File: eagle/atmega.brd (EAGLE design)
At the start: 65.3 x 40.9 mm, 48 parts, among them IC1 TO 5V, IC2 LM339D, Q2 16MHz, U1 ATMEGA328P-AU

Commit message: Dopisanie kilku komentarzy do schematu
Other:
- board size 65.3 x 40.9 mm -> 65.3 x 43.7 mm

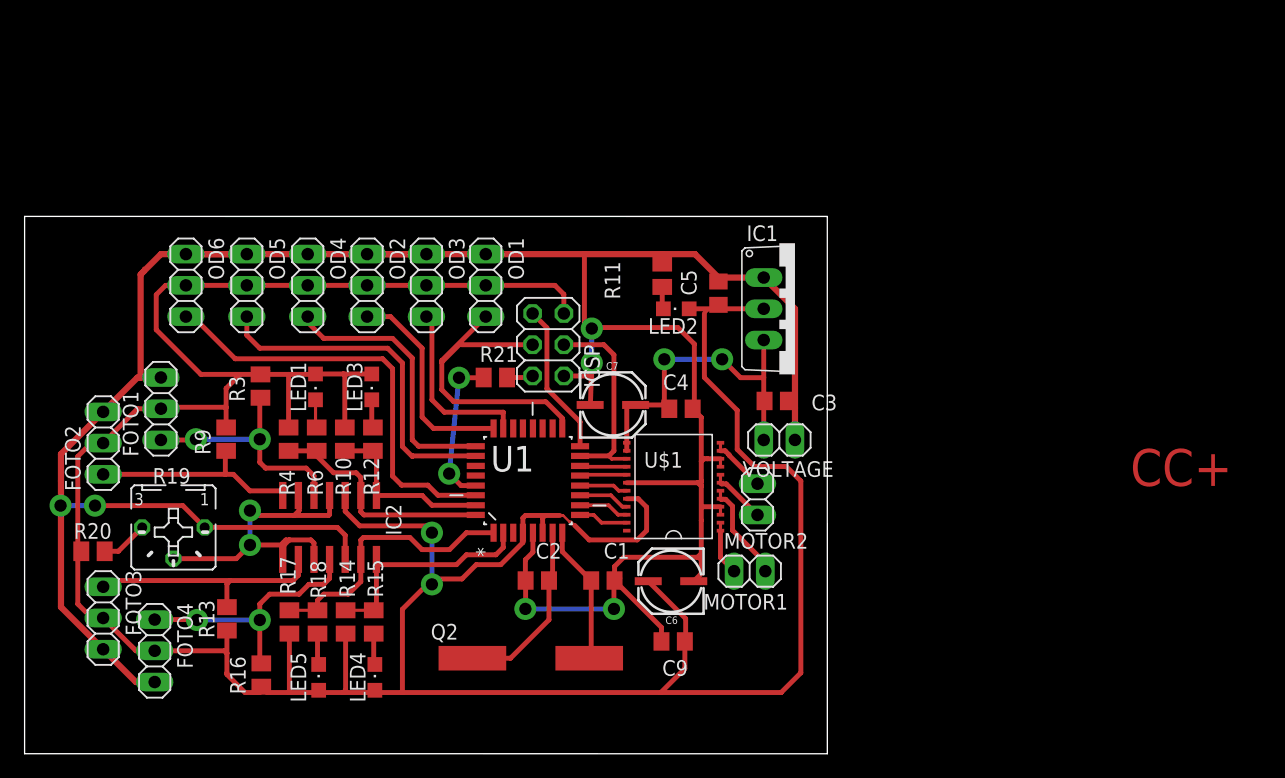
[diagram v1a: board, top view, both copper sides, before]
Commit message: usunięcie LEDów
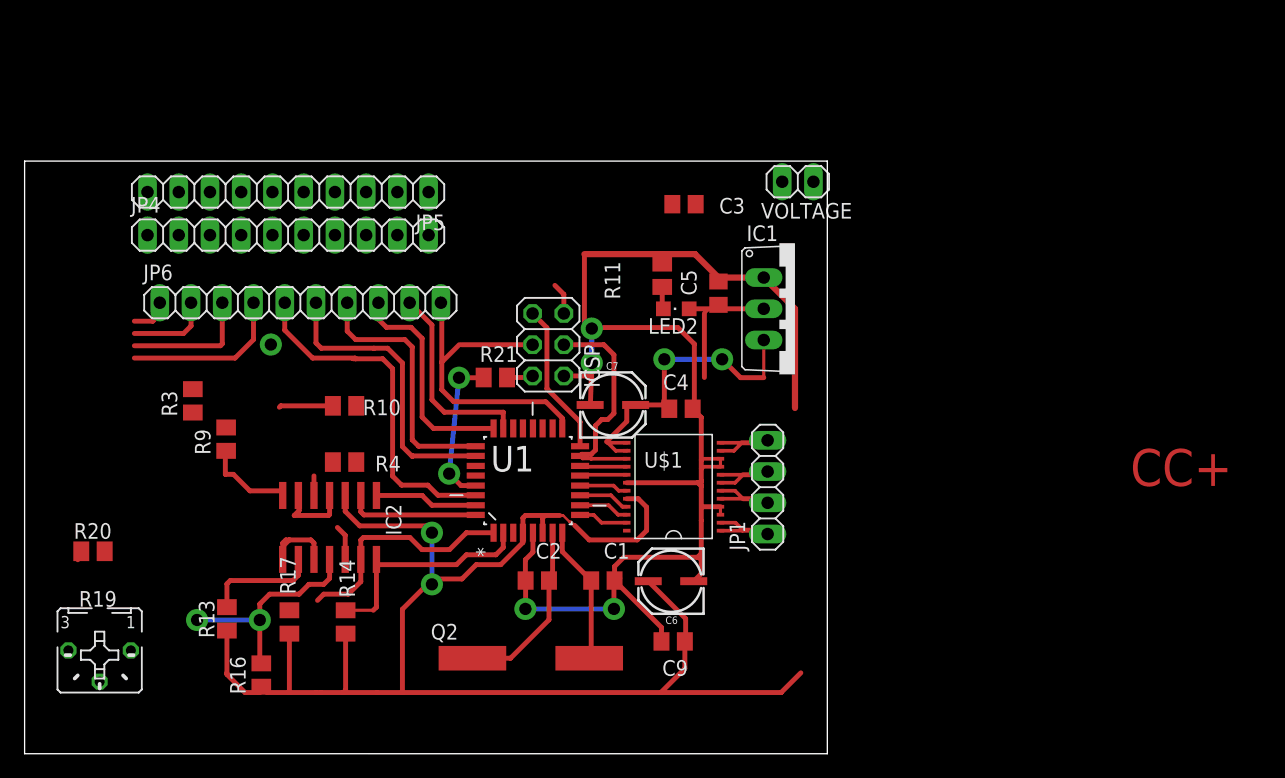
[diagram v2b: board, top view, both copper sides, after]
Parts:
- removed FOTO1, FOTO2, FOTO3, FOTO4, OD1, OD2, OD3, OD4, OD5, OD6: (no value), pinhead:1X03
- removed LED1, LED3, LED4, LED5: (no value), led:CHIPLED_0805
- removed MOTOR1, MOTOR2: (no value), pinhead:1X02
- removed R12, R15, R18, R6: 220R, resistor:M0805
- added JP1: (no value), pinhead:1X04
- added JP4, JP5, JP6: (no value), pinhead:1X10
- moved VOLTAGE 21.1 mm to (61.0, 42.3)
- moved C3 17.7 mm to (51.7, 40.5)
- moved R19 11.7 mm to (4.18, 4.23)
- moved R3 5.63 mm to (11.8, 24.5)
- moved R4 4.92 mm to (24.1, 19.5), turned to 180 degrees
- moved R10 2.71 mm to (24.1, 24.1), turned to 180 degrees
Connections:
- removed net N$2: LED3.C, R12.2
- removed net N$20: LED1.C, R6.2
- removed net N$21: LED4.C, R15.2
- removed net N$29: LED5.C, R18.2
- removed net OUTMA1: MOTOR1.2, U$1.1, U$1.2
- removed net OUTMA2: MOTOR1.1, U$1.5, U$1.6
- removed net OUTMB1: MOTOR2.1, U$1.11, U$1.12
- removed net OUTMB2: MOTOR2.2, U$1.7, U$1.8
- new net AO1: JP1.1, U$1.1, U$1.2
- new net AO2: JP1.2, U$1.5, U$1.6
- new net BO1: JP1.4, U$1.11, U$1.12
- new net BO2: JP1.3, U$1.7, U$1.8
- net CO1: now also JP6.10; no longer OD1.3
- net CO2: now also JP6.8; no longer OD2.3
- net CO3: now also JP6.9; no longer OD3.3
- net CO4: now also JP6.7; no longer OD4.3
- net CO5: now also JP6.6; no longer OD5.3
- net CO6: now also JP6.5; no longer OD6.3
- net GND: now also JP5.10; no longer FOTO1.3, FOTO2.3, FOTO3.3, FOTO4.3, OD1.1, OD2.1, OD3.1, OD4.1, OD5.1, OD6.1
- net KO1: no longer R6.1
- net KO2: no longer R12.1
- net KO3: no longer R15.1
- net KO4: no longer R18.1
- net KOM1: now also JP6.4; no longer FOTO1.1
- net KOM2: now also JP6.3; no longer FOTO2.1
- net KOM3: now also JP6.1; no longer FOTO3.1
- net KOM4: now also JP6.2; no longer FOTO4.1
- net VCC: now also JP4.10; no longer FOTO1.2, FOTO2.2, FOTO3.2, FOTO4.2, LED1.A, LED3.A, LED4.A, LED5.A, OD1.2, OD2.2, OD3.2, OD4.2, OD5.2, OD6.2
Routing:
- net VCC: track 306.5 -> 152.3 mm
- net GND: track 244.1 -> 126.6 mm, vias 6 -> 4
- net POT: track 28.8 -> 12.8 mm, vias 2 -> 0
- net VZ: track 37.6 -> 28.0 mm
- net KO1: track 19.3 -> 10.8 mm
- net OUTMA2: track 8.27 -> 0.00 mm
- net KOM3: track 20.9 -> 13.0 mm
- net BO1: track 0.00 -> 7.48 mm
- net BO2: track 0.00 -> 7.47 mm
- net AO1: track 0.00 -> 7.39 mm
- net AO2: track 0.00 -> 7.36 mm
- net CO6: track 34.7 -> 28.7 mm
- net KO2: track 14.4 -> 8.78 mm
- net KOM1: track 19.8 -> 14.9 mm, vias 2 -> 0
- net OUTMB1: track 4.80 -> 0.00 mm
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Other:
- board size 65.3 x 43.7 mm -> 65.3 x 48.2 mm
